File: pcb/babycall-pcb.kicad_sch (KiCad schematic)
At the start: 35 parts, among them SW1 TS-1187A-B-A-B, SW2 TS-1187A-B-A-B, U1 ESP32-C3-MINI-1-H4X, U2 BQ24074RGTR, U3 AP2112K-3.3, U4 ICS-43434_C5656610

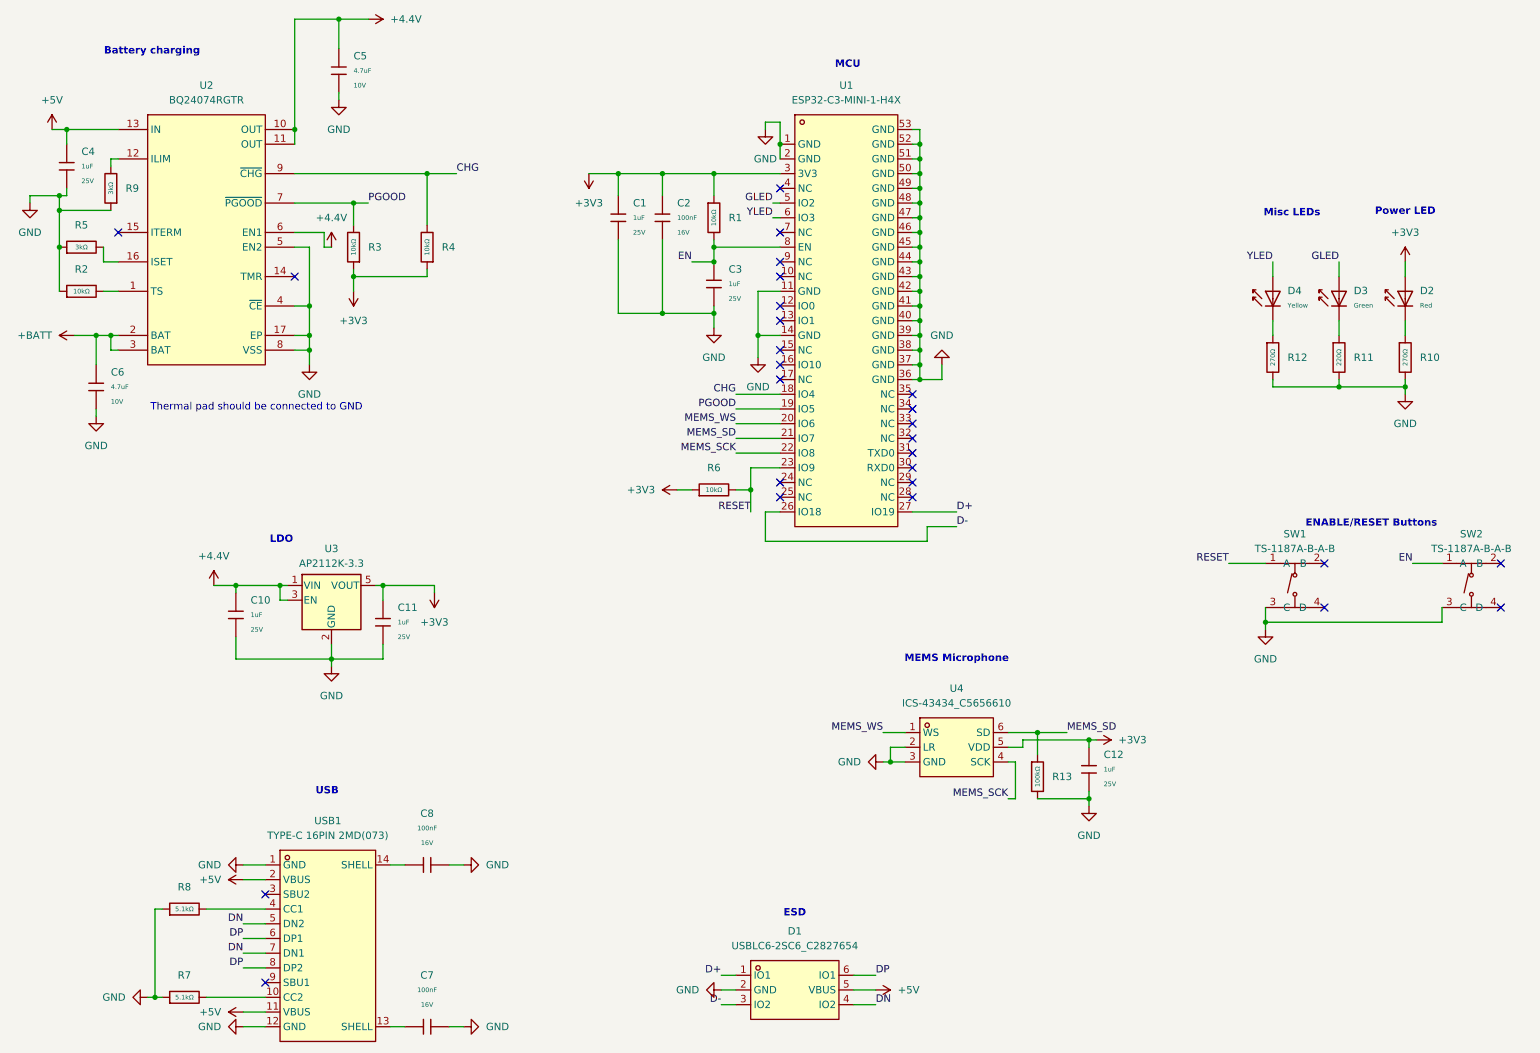
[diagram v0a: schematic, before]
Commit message: Claude stuff, and gitignore
Also some models for pcb
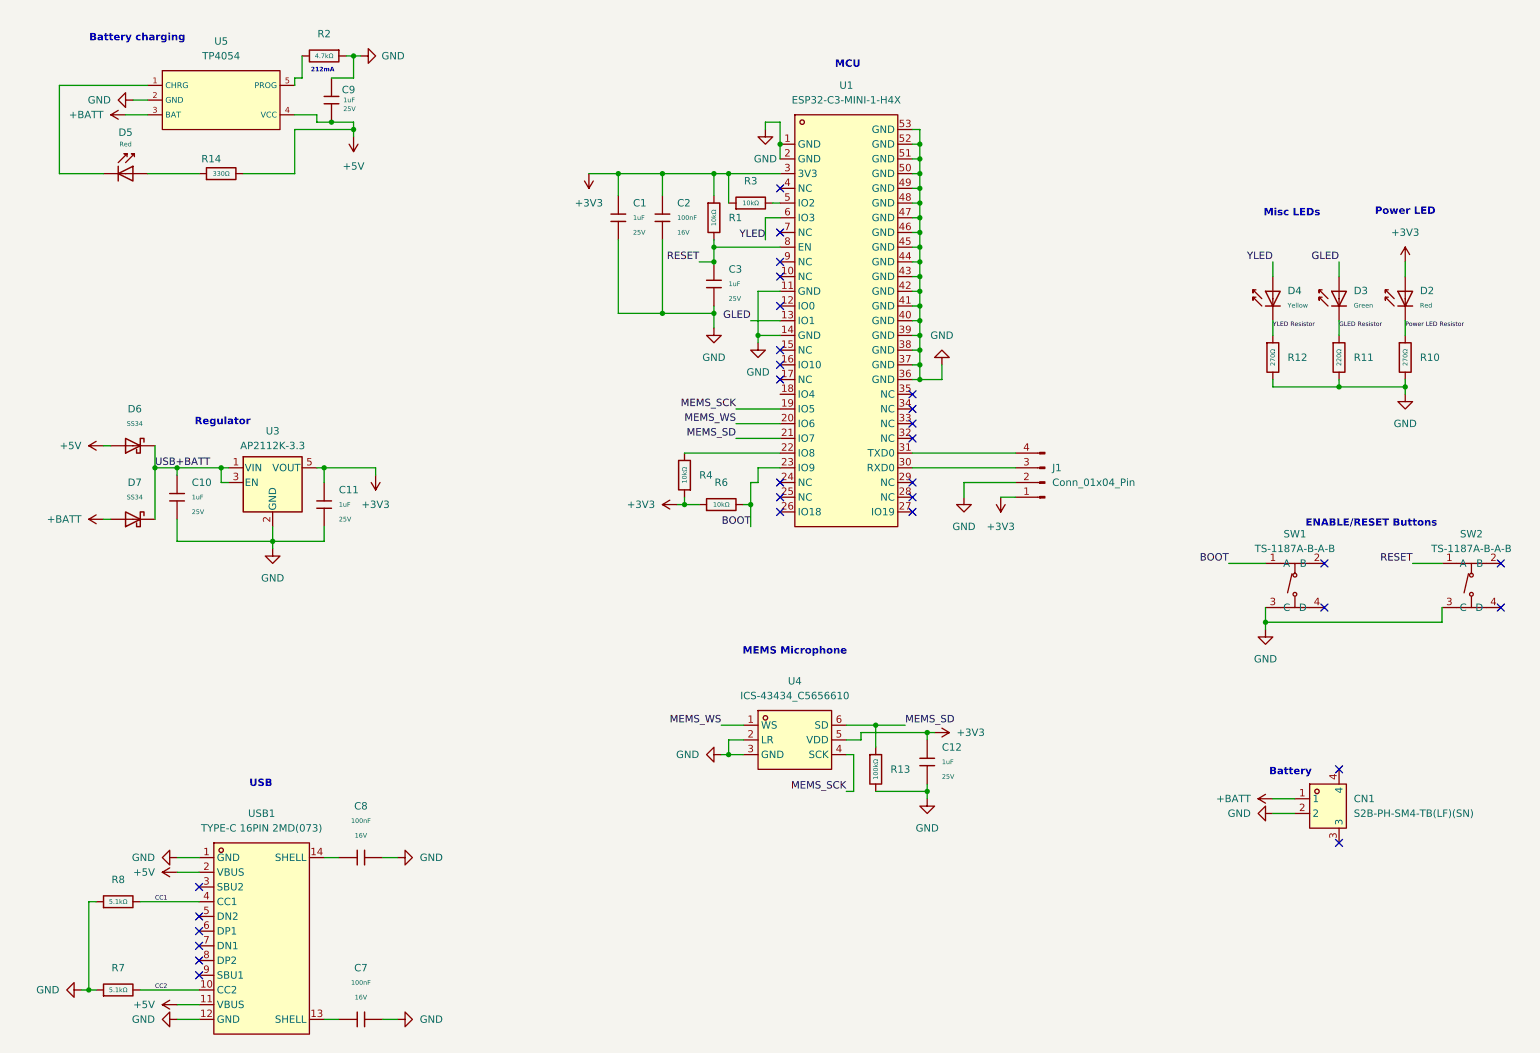
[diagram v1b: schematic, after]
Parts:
- removed C4: 1uF, PCM_JLCPCB:C_0402, symbol PCM_JLCPCB-Capacitors:0402,1uF
- removed C5, C6: 4.7uF, PCM_JLCPCB:C_0402, symbol PCM_JLCPCB-Capacitors:0402,4.7uF
- removed D1: USBLC6-2SC6_C2827654, jlcpcb:SOT-23-6_L2.9-W1.6-P0.95-LS2.8-BL, symbol JLCPCB:USBLC6-2SC6_C2827654
- removed R2: 10kΩ, PCM_JLCPCB:R_0402, symbol PCM_JLCPCB-Resistors:0402,10kΩ
- removed R5, R9: 3kΩ, PCM_JLCPCB:R_0603, symbol PCM_JLCPCB-Resistors:0603,3kΩ
- removed U2: BQ24074RGTR, jlcpcb:QFN-16_L3.0-W3.0-P0.50-TL-EP1.7, symbol JLCPCB:BQ24074RGTR
- added C9: 1uF, PCM_JLCPCB:C_0402, symbol PCM_JLCPCB-Capacitors:0402,1uF
- added CN1: S2B-PH-SM4-TB(LF)(SN), jlcpcb:CONN-SMD_P2.00_S2B-PH-SM4-TB-LF-SN, symbol JLCPCB:S2B-PH-SM4-TB(LF)(SN)
- added D5: Red, PCM_JLCPCB:D_0603, symbol PCM_JLCPCB-Diodes:LED,0603,Red
- added D6, D7: SS34, PCM_JLCPCB:D_SMA, symbol PCM_JLCPCB-Diodes:Schottky,SS34,(2)
- added J1: Conn_01x04_Pin, Connector_PinHeader_2.54mm:PinHeader_1x04_P2.54mm_Vertical, symbol Connector:Conn_01x04_Pin
- added R14: 330Ω, PCM_JLCPCB:R_0402, symbol PCM_JLCPCB-Resistors:0402,330Ω
- added R2: 4.7kΩ, PCM_JLCPCB:R_0402, symbol PCM_JLCPCB-Resistors:0402,4.7kΩ
- added U5: TP4054, PCM_JLCPCB:SOT-23-5_L3.0-W1.7-P0.95-LS2.8-BL, symbol PCM_JLCPCB-Power:Battery, Li-Ion, 0.8A, TP4054
- C1, C10, C11, C12, C3: LCSC C52923 -> (none); LCSC Part Number (none) -> C52923
- C2, C7, C8: LCSC C1525 -> (none); LCSC Part Number (none) -> C1525
- D2: LCSC C2286 -> (none); LCSC Part Number (none) -> C2286
- D3: LCSC C2297 -> (none); LCSC Part Number (none) -> C2297
- D4: LCSC C89811 -> (none); LCSC Part Number (none) -> C89811
- R1, R3, R4, R6: LCSC C25744 -> (none); LCSC Part Number (none) -> C25744
- R10, R12: LCSC C22966 -> (none); LCSC Part Number (none) -> C22966
- R11: LCSC C25091 -> (none); LCSC Part Number (none) -> C25091
- R13: LCSC C25741 -> (none); LCSC Part Number (none) -> C25741
- R7, R8: LCSC C25905 -> (none); LCSC Part Number (none) -> C25905
- SW1, SW2: LCSC Part C318884 -> (none); LCSC Part Number (none) -> C318884
- U1: LCSC Part C41349510 -> (none); LCSC Part Number (none) -> C41349510
- U3: LCSC Part Number (none) -> C23380830
- U4: LCSC Part C5656610 -> (none); LCSC Part Number (none) -> C5656610
- USB1: LCSC Part C2765186 -> (none); LCSC Part Number (none) -> C2765186
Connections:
- net EN is gone; now on net RESET: C3.1, R1.2, SW2.1 (A), U1.8 (EN)
- net +3V3: now also J1.1 (Pin_1)
- net +5V: now also C9.2, D6.2, R14.2, U5.4 (VCC)
- net +BATT: now also CN1.1, D7.2, U5.3 (BAT)
- net GLED: now also U1.13 (IO1); no longer U1.5 (IO2)
- net GND: now also C9.1, CN1.2, J1.2 (Pin_2), R2.1, U5.2 (GND)
- net MEMS_SCK: now also U1.19 (IO5); no longer U1.22 (IO8)
- net RESET: no longer R6.2, SW1.1 (A), U1.23 (IO9)
- net GLED Resistor: now reaches D3.1, R11.1
- net CC1: now reaches R8.2, USB1.4 (CC1)
- net Power LED Resistor: now reaches D2.1, R10.1
- net CC2: now reaches R7.2, USB1.10 (CC2)
- net YLED Resistor: now reaches D4.1, R12.1
- net at U1.30 (RXD0): now also J1.3 (Pin_3)
- net at U1.31 (TXD0): now also J1.4 (Pin_4)
- net +4.4V renamed USB+BATT
- net USB+BATT: now also D6.1, D7.1
- net CHG: no longer names the net of R4.2
- net CHG: now also U1.22 (IO8); no longer U1.18 (IO4)
- net D+: no longer names the net of U1.27 (IO19)
- net D-: no longer names the net of U1.26 (IO18)
- net DN: no longer names the net of USB1.5 (DN2)
- net DN: no longer USB1.7 (DN1)
- net DP: no longer names the net of USB1.6 (DP1)
- net DP: no longer USB1.8 (DP2)
- net PGOOD: no longer names the net of R3.2
- net PGOOD: now also U1.5 (IO2); no longer U1.19 (IO5)
- new net: R2.2, U5.5 (PROG)
- new net: D5.2, R14.1
- new net: D5.1, U5.1 (CHRG)
- new net BOOT: R6.2, SW1.1 (A), U1.23 (IO9)
- no-connect marks 27 -> 30
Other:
- note added: "212mA"
- note added: "Battery"
- note added: "Regulator"
- note removed: "ESD"
- note removed: "LDO"
- note removed: "Thermal pad should be connected to GND"
- moved on the sheet: C10, C11, C12, C7, C8, R13, R6, R7, R8, U3, U4, USB1
